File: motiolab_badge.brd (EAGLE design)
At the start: 89.6 x 79.8 mm, 0 parts

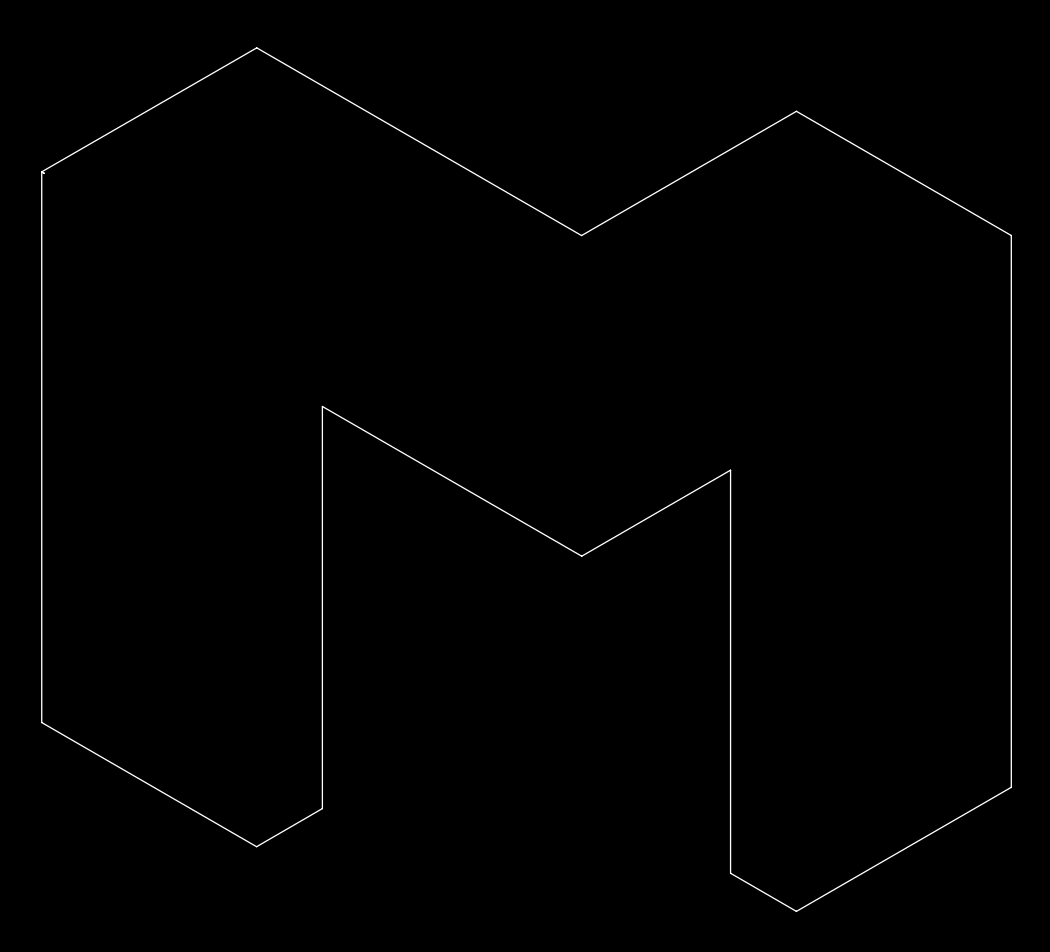
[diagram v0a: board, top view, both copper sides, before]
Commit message: Add ESP32-WROOM to schematic. Create ground planes and appropiate restrict shapes to match the board contour.
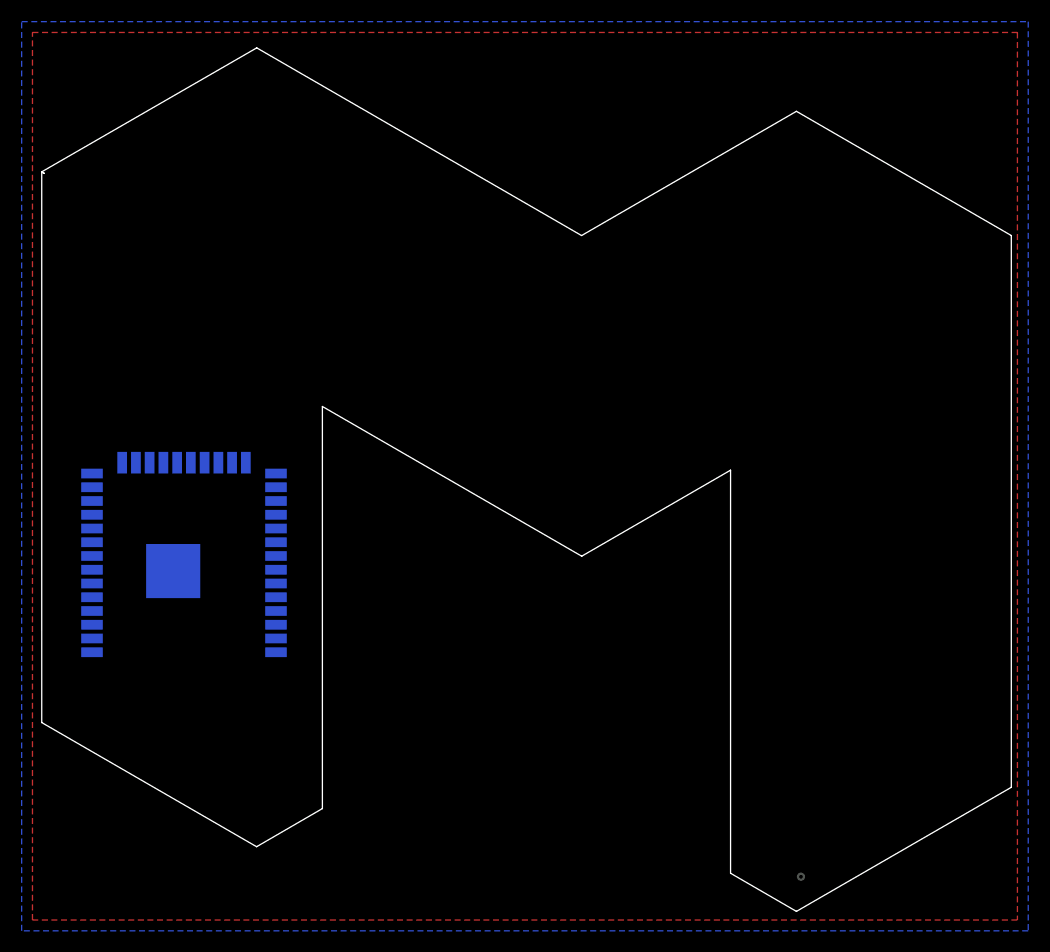
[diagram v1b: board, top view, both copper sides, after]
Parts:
- added U1: ESP32-WROOM-32D, ML_badge:MODULE_ESP32-WROOM-32D
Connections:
- new net +3V3: U1.2
- new net GND: U1.1, U1.15, U1.38, U1.39
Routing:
- added copper zone on layer 1, net GND
- added copper zone on layer 16, net GND
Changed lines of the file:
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@@
 <setting verticaltext="up"/>
 </settings>
-<grid distance="1" unitdist="mm" unit="mm" style="lines" multiple="1" display="no" altdistance="5" altunitdist="mil" altunit="mil"/>
+<grid distance="0.1" unitdist="mm" unit="mm" style="lines" multiple="1" display="no" altdistance="5" altunitdist="mil" altunit="mil"/>
 <layers>
 <layer number="1" name="Top" color="4" fill="1" visible="yes" active="yes"/>
@@
 <layer number="39" name="tKeepout" color="4" fill="11" visible="yes" active="yes"/>
 <layer number="40" name="bKeepout" color="1" fill="11" visible="yes" active="yes"/>
-<layer number="41" name="tRestrict" color="4" fill="10" visible="yes" active="yes"/>
-<layer number="42" name="bRestrict" color="1" fill="10" visible="yes" active="yes"/>
+<layer number="41" name="tRestrict" color="4" fill="10" visible="no" active="yes"/>
+<layer number="42" name="bRestrict" color="1" fill="10" visible="no" active="yes"/>
 <layer number="43" name="vRestrict" color="2" fill="10" visible="yes" active="yes"/>
 <layer number="44" name="Drills" color="7" fill="1" visible="no" active="yes"/>
@@
 <wire x1="90.43548125" y1="12.259759375" x2="90.43548125" y2="63.23903125" width="0.001" layer="20"/>
 <wire x1="90.43548125" y1="63.23903125" x2="70.58403125" y2="74.71563125" width="0.001" layer="20"/>
+<polygon width="0.2" layer="29">
+<vertex x="20.7" y="74.9"/>
+<vertex x="50.7" y="57.6"/>
+<vertex x="70.6" y="69"/>
+<vertex x="80.6" y="63.2"/>
+<vertex x="50.7" y="46"/>
+<vertex x="10.8" y="69.1"/>
+</polygon>
+<polygon width="0.2" layer="42">
+<vertex x="20.7" y="74.9"/>
+<vertex x="50.8" y="57.5"/>
+<vertex x="70.6" y="69"/>
+<vertex x="80.6" y="63.2"/>
+<vertex x="50.7" y="46"/>
+<vertex x="10.7" y="69.2"/>
+</polygon>
 </plain>
 <attributes>
@@
 </autorouter>
 <elements>
+<element name="U1" library="ML_badge" package="MODULE_ESP32-WROOM-32D" value="ESP32-WROOM-32D" x="14" y="30" smashed="yes" rot="MR180">
+<attribute name="AVAILABILITY" value="Unavailable" x="14" y="30" size="1.778" layer="28" rot="MR180" display="off"/>
+<attribute name="DISTRIBUTOR" value="Mouser" x="14" y="30" size="1.778" layer="28" rot="MR180" display="off"/>
+<attribute name="DISTRUBUTOR_REF" value="356-ESP32WROOM-32D" x="14" y="30" size="1.778" layer="28" rot="MR180" display="off"/>
+<attribute name="MANUFACTURER" value="Espressif Systems" x="14" y="30" size="1.778" layer="28" rot="MR180" display="off"/>
+<attribute name="MANUFACTURER_REF" value="ESP32-WROOM-32D" x="14" y="30" size="1.778" layer="28" rot="MR180" display="off"/>
+<attribute name="NAME" x="5.7167" y="16.1581" size="1.27341875" layer="26" rot="MR180"/>
+<attribute name="VALUE" x="5.033040625" y="45.6155" size="1.2738" layer="28" rot="MR180"/>
+</element>
 </elements>
 <signals>
+<signal name="GND">
+<contactref element="U1" pad="15"/>
+<contactref element="U1" pad="1"/>
+<contactref element="U1" pad="39"/>
+<contactref element="U1" pad="38"/>
+<polygon width="0.1524" layer="1">
+<vertex x="0" y="82"/>
+<vertex x="91" y="82"/>
+<vertex x="91" y="0"/>
+<vertex x="0" y="0"/>
+</polygon>
+<polygon width="0.2" layer="16">
+<vertex x="-1" y="83"/>
+<vertex x="92" y="83"/>
+<vertex x="92" y="-1"/>
+<vertex x="-1" y="-1"/>
+</polygon>
+<via x="71" y="4" extent="1-16" drill="0.35"/>
+</signal>
+<signal name="+3V3">
+<contactref element="U1" pad="2"/>
+</signal>
 </signals>
 <mfgpreviewcolors>
